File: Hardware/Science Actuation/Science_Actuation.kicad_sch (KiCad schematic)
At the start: 110 parts, among them J1 Conn_01x03_Pin, J2 Conn_01x03_Pin, J2 RJ45_LED_Shielded, J3 Conn_01x03_Pin, Q1 BSS138, Q10 AO3401A, Q9 BSS138, SW1 SW_Push, SW10 SW_SPDT, SW2 SW_Push, SW3 SW_Push, SW4 SW_Push, SW5 SW_Push, SW6 SW_Push, SW7 SW_Push, SW8 SW_Push, SW9 SW_Push, U2 OKI, U2 Teensy4.1_DEV-16771

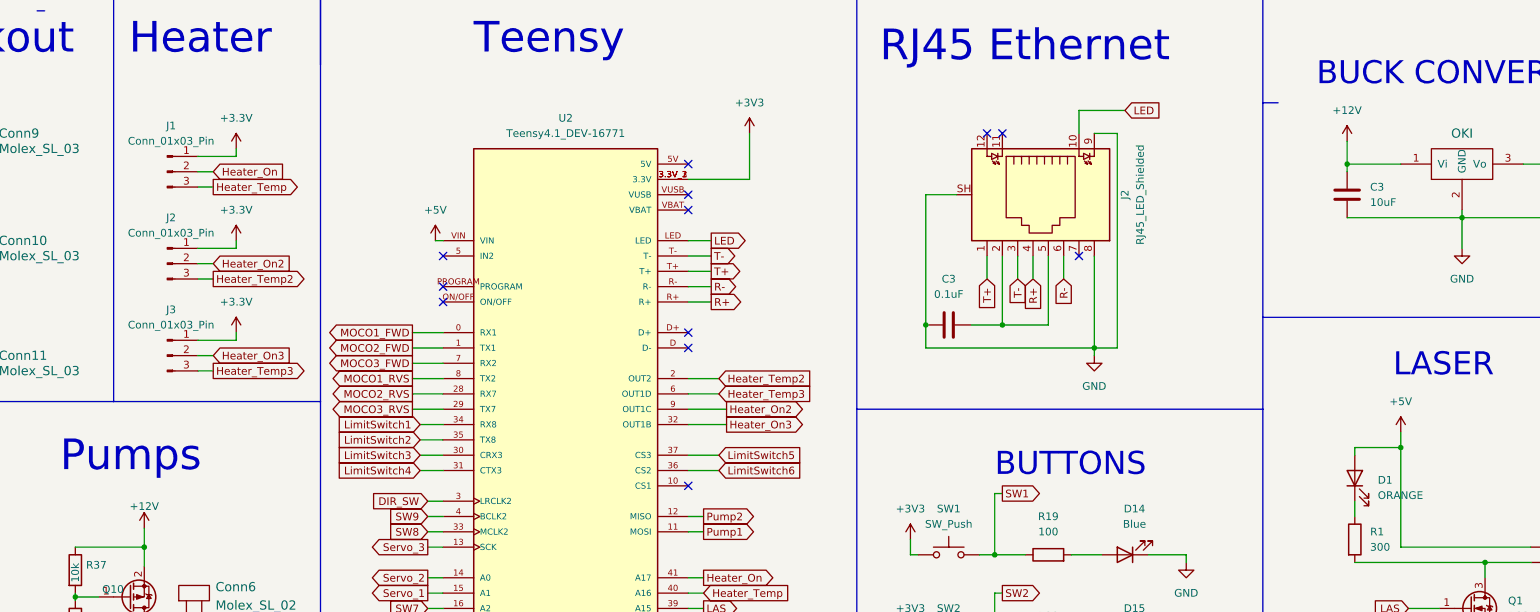
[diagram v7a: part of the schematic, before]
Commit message: Changed 3-pin connectors to Molexes
Added footnotes to the new molexes as well
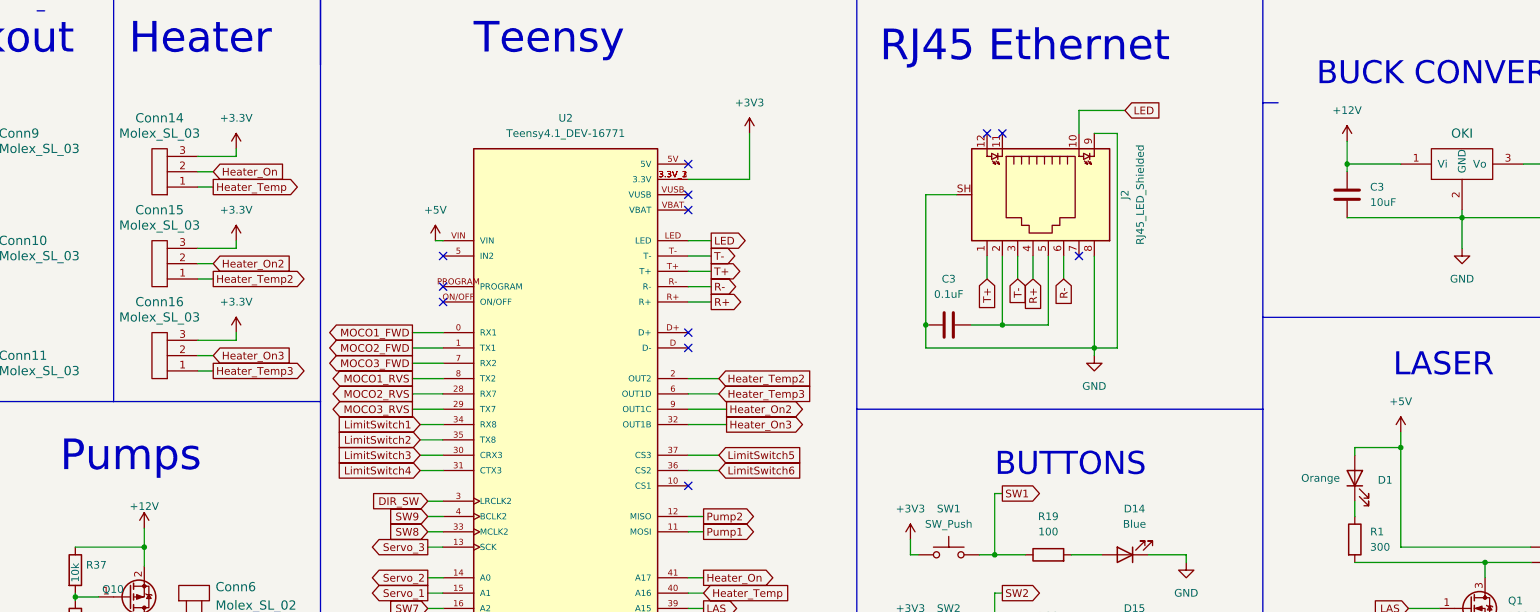
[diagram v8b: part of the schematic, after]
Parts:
- removed J1, J2, J3: Conn_01x03_Pin, MRDT_Connectors:MOLEX_SL_03_Horizontal, symbol Connector:Conn_01x03_Pin
- added Conn14, Conn15, Conn16: Molex_SL_03, MRDT_Connectors:MOLEX_SL_03_Vertical, symbol MRDT_Connectors:Molex_SL_03
- D1: value ORANGE -> Orange
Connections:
- net +3.3V: now also Conn14.3, Conn15.3, Conn16.3
- net Heater_On: now also Conn14.2
- net Heater_On2: now also Conn15.2
- net Heater_On3: now also Conn16.2
- net Heater_Temp: now also Conn14.1
- net Heater_Temp2: now also Conn15.1
- net Heater_Temp3: now also Conn16.1
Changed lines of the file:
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@@
     (stroke (width 0) (type default))
   )
+  (wire (pts (xy 133.35 41.91) (xy 135.89 41.91))
+    (stroke (width 0) (type default))
+  )
   (wire (pts (xy 170.18 83.82) (xy 173.99 83.82))
     (stroke (width 0) (type default))
@@
     (stroke (width 0) (type default))
   )
+  (wire (pts (xy 133.35 59.69) (xy 135.89 59.69))
+    (stroke (width 0) (type default))
+  )
   (wire (pts (xy 251.46 226.06) (xy 252.73 226.06))
     (stroke (width 0) (type default))
@@
     (stroke (width 0) (type default))
   )
+  (wire (pts (xy 133.35 57.15) (xy 135.89 57.15))
+    (stroke (width 0) (type default))
+  )
   (wire (pts (xy 251.46 156.21) (xy 252.73 156.21))
     (stroke (width 0) (type default))
@@
     (stroke (width 0) (type default))
   )
-  (wire (pts (xy 133.35 72.39) (xy 135.89 72.39))
-    (stroke (width 0) (type default))
-  )
   (wire (pts (xy 204.47 176.53) (xy 213.36 176.53))
     (stroke (width 0) (type default))
@@
     (stroke (width 0) (type default))
   )
+  (wire (pts (xy 133.35 39.37) (xy 139.7 39.37))
+    (stroke (width 0) (type default))
+  )
   (wire (pts (xy 53.34 191.77) (xy 57.15 191.77))
     (stroke (width 0) (type default))
@@
     (stroke (width 0) (type default))
   )
-  (wire (pts (xy 133.35 74.93) (xy 135.89 74.93))
-    (stroke (width 0) (type default))
-  )
   (wire (pts (xy 265.43 181.61) (xy 265.43 191.77))
     (stroke (width 0) (type default))
@@
     (stroke (width 0) (type default))
   )
+  (wire (pts (xy 133.35 74.93) (xy 135.89 74.93))
+    (stroke (width 0) (type default))
+  )
   (wire (pts (xy 171.45 109.22) (xy 173.99 109.22))
     (stroke (width 0) (type default))
@@
     (stroke (width 0) (type default))
   )
-  (wire (pts (xy 133.35 57.15) (xy 135.89 57.15))
-    (stroke (width 0) (type default))
-  )
   (wire (pts (xy 113.03 112.395) (xy 116.84 112.395))
     (stroke (width 0) (type default))
   )
-  (wire (pts (xy 133.35 44.45) (xy 135.89 44.45))
-    (stroke (width 0) (type default))
-  )
   (polyline (pts (xy 153.67 237.49) (xy 242.57 237.49))
     (stroke (width 0) (type default))
@@
     (stroke (width 0) (type default))
   )
-  (wire (pts (xy 139.7 39.37) (xy 133.35 39.37))
-    (stroke (width 0) (type default))
-  )
   (wire (pts (xy 346.71 119.38) (xy 346.71 123.19))
     (stroke (width 0) (type default))
@@
     (stroke (width 0) (type default))
   )
+  (wire (pts (xy 133.35 54.61) (xy 139.7 54.61))
+    (stroke (width 0) (type default))
+  )
   (wire (pts (xy 251.46 172.72) (xy 251.46 175.26))
     (stroke (width 0) (type default))
@@
     (stroke (width 0) (type default))
   )
-  (wire (pts (xy 139.7 54.61) (xy 133.35 54.61))
-    (stroke (width 0) (type default))
-  )
   (wire (pts (xy 34.29 118.11) (xy 27.94 118.11))
     (stroke (width 0) (type default))
@@
     (stroke (width 0) (type default))
   )
+  (wire (pts (xy 133.35 72.39) (xy 135.89 72.39))
+    (stroke (width 0) (type default))
+  )
   (wire (pts (xy 171.45 124.46) (xy 173.99 124.46))
     (stroke (width 0) (type default))
@@
     (stroke (width 0) (type default))
   )
-  (wire (pts (xy 139.7 69.85) (xy 133.35 69.85))
-    (stroke (width 0) (type default))
-  )
   (wire (pts (xy 136.525 118.11) (xy 136.525 129.54))
     (stroke (width 0) (type default))
@@
     (stroke (width 0) (type default))
   )
+  (wire (pts (xy 133.35 69.85) (xy 139.7 69.85))
+    (stroke (width 0) (type default))
+  )
+  (wire (pts (xy 133.35 44.45) (xy 135.89 44.45))
+    (stroke (width 0) (type default))
+  )
   (wire (pts (xy 53.34 218.44) (xy 57.15 218.44))
     (stroke (width 0) (type default))
@@
     (stroke (width 0) (type default))
   )
-  (wire (pts (xy 133.35 41.91) (xy 135.89 41.91))
-    (stroke (width 0) (type default))
-  )
   (polyline (pts (xy 309.88 12.7) (xy 309.88 81.28))
     (stroke (width 0) (type default))
@@
     (stroke (width 0) (type default))
   )
-  (wire (pts (xy 133.35 59.69) (xy 135.89 59.69))
-    (stroke (width 0) (type default))
-  )
   (wire (pts (xy 265.43 232.41) (xy 265.43 242.57))
     (stroke (width 0) (type default))
@@
   )
   (symbol (lib_id "Device:LED") (at 325.12 92.71 90) (unit 1)
-    (in_bom yes) (on_board yes) (dnp no) (fields_autoplaced)
+    (in_bom yes) (on_board yes) (dnp no)
     (property "Reference" "D1" (at 328.93 93.0275 90)
       (effects (font (size 1.27 1.27)) (justify right))
     )
-    (property "Value" "ORANGE" (at 328.93 95.5675 90)
+    (property "Value" "Orange" (at 316.23 92.71 90)
       (effects (font (size 1.27 1.27)) (justify right))
     )
@@
     )
   )
-  (symbol (lib_id "Connector:Conn_01x03_Pin") (at 128.27 41.91 0) (unit 1)
+  (symbol (lib_id "MRDT_Connectors:Molex_SL_03") (at 128.27 38.1 180) (unit 1)
     (in_bom yes) (on_board yes) (dnp no) (fields_autoplaced)
-    (property "Reference" "J1" (at 128.905 34.29 0)
-      (effects (font (size 1.27 1.27)))
+    (property "Reference" "Conn14" (at 127 33.02 0)
+      (effects (font (size 1.524 1.524)))
     )
-    (property "Value" "Conn_01x03_Pin" (at 128.905 36.83 0)
-      (effects (font (size 1.27 1.27)))
+    (property "Value" "Molex_SL_03" (at 127 35.56 0)
+      (effects (font (size 1.524 1.524)))
     )
-    (property "Footprint" "MRDT_Connectors:MOLEX_SL_03_Horizontal" (at 128.27 41.91 0)
-      (effects (font (size 1.27 1.27)) hide)
+    (property "Footprint" "MRDT_Connectors:MOLEX_SL_03_Vertical" (at 128.27 38.1 0)
+      (effects (font (size 1.524 1.524)) hide)
     )
-    (property "Datasheet" "~" (at 128.27 41.91 0)
-      (effects (font (size 1.27 1.27)) hide)
+    (property "Datasheet" "" (at 128.27 38.1 0)
+      (effects (font (size 1.524 1.524)) hide)
     )
     (pin "1")
@@
       (project "Science_Actuation"
         (path "/a309c31d-a907-45c3-9170-b69a69763088"
-          (reference "J1") (unit 1)
+          (reference "Conn14") (unit 1)
         )
       )
@@
     )
   )
-  (symbol (lib_id "Connector:Conn_01x03_Pin") (at 128.27 57.15 0) (unit 1)
-    (in_bom yes) (on_board yes) (dnp no) (fields_autoplaced)
-    (property "Reference" "J2" (at 128.905 49.53 0)
-      (effects (font (size 1.27 1.27)))
-    )
-    (property "Value" "Conn_01x03_Pin" (at 128.905 52.07 0)
-      (effects (font (size 1.27 1.27)))
-    )
-    (property "Footprint" "MRDT_Connectors:MOLEX_SL_03_Horizontal" (at 128.27 57.15 0)
-      (effects (font (size 1.27 1.27)) hide)
-    )
-    (property "Datasheet" "~" (at 128.27 57.15 0)
-      (effects (font (size 1.27 1.27)) hide)
-    )
-    (pin "1")
-    (pin "2")
-    (pin "3")
-    (instances
-      (project "Science_Actuation"
-        (path "/a309c31d-a907-45c3-9170-b69a69763088"
-          (reference "J2") (unit 1)
-        )
-      )
-    )
-  )
   (symbol (lib_id "power:GND") (at 116.84 233.68 0) (unit 1)
     (in_bom yes) (on_board yes) (dnp no) (fields_autoplaced)
@@
     )
   )
-  (symbol (lib_id "Connector:Conn_01x03_Pin") (at 128.27 72.39 0) (unit 1)
-    (in_bom yes) (on_board yes) (dnp no) (fields_autoplaced)
-    (property "Reference" "J3" (at 128.905 64.77 0)
-      (effects (font (size 1.27 1.27)))
-    )
-    (property "Value" "Conn_01x03_Pin" (at 128.905 67.31 0)
-      (effects (font (size 1.27 1.27)))
-    )
-    (property "Footprint" "MRDT_Connectors:MOLEX_SL_03_Horizontal" (at 128.27 72.39 0)
-      (effects (font (size 1.27 1.27)) hide)
-    )
-    (property "Datasheet" "~" (at 128.27 72.39 0)
-      (effects (font (size 1.27 1.27)) hide)
-    )
-    (pin "1")
-    (pin "2")
-    (pin "3")
-    (instances
-      (project "Science_Actuation"
-        (path "/a309c31d-a907-45c3-9170-b69a69763088"
-          (reference "J3") (unit 1)
-        )
-      )
-    )
-  )
   (symbol (lib_id "Device:R") (at 274.32 105.41 90) (unit 1)
     (in_bom yes) (on_board yes) (dnp no) (fields_autoplaced)
@@
     )
   )
+  (symbol (lib_id "MRDT_Connectors:Molex_SL_03") (at 128.27 53.34 180) (unit 1)
+    (in_bom yes) (on_board yes) (dnp no) (fields_autoplaced)
+    (property "Reference" "Conn15" (at 127 48.26 0)
+      (effects (font (size 1.524 1.524)))
+    )
+    (property "Value" "Molex_SL_03" (at 127 50.8 0)
+      (effects (font (size 1.524 1.524)))
+    )
+    (property "Footprint" "MRDT_Connectors:MOLEX_SL_03_Vertical" (at 128.27 53.34 0)
+      (effects (font (size 1.524 1.524)) hide)
+    )
+    (property "Datasheet" "" (at 128.27 53.34 0)
+      (effects (font (size 1.524 1.524)) hide)
+    )
+    (pin "1")
+    (pin "2")
+    (pin "3")
+    (instances
+      (project "Science_Actuation"
+        (path "/a309c31d-a907-45c3-9170-b69a69763088"
+          (reference "Conn15") (unit 1)
+        )
+      )
+    )
+  )
   (symbol (lib_id "Device:R") (at 274.32 156.21 90) (unit 1)
     (in_bom yes) (on_board yes) (dnp no) (fields_autoplaced)
@@
         )
       )
+    )
+  )
+  (symbol (lib_id "MRDT_Connectors:Molex_SL_03") (at 128.27 68.58 180) (unit 1)
+    (in_bom yes) (on_board yes) (dnp no) (fields_autoplaced)
+    (property "Reference" "Conn16" (at 127 63.5 0)
+      (effects (font (size 1.524 1.524)))
+    )
+    (property "Value" "Molex_SL_03" (at 127 66.04 0)
+      (effects (font (size 1.524 1.524)))
+    )
+    (property "Footprint" "MRDT_Connectors:MOLEX_SL_03_Vertical" (at 128.27 68.58 0)
+      (effects (font (size 1.524 1.524)) hide)
+    )
+    (property "Datasheet" "" (at 128.27 68.58 0)
+      (effects (font (size 1.524 1.524)) hide)
+    )
+    (pin "1")
+    (pin "2")
+    (pin "3")
+    (instances
+      (project "Science_Actuation"
+        (path "/a309c31d-a907-45c3-9170-b69a69763088"
+          (reference "Conn16") (unit 1)
+        )
+      )
